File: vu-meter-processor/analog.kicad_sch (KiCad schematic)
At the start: 52 parts, among them U1 LM2904, U2 LM2904

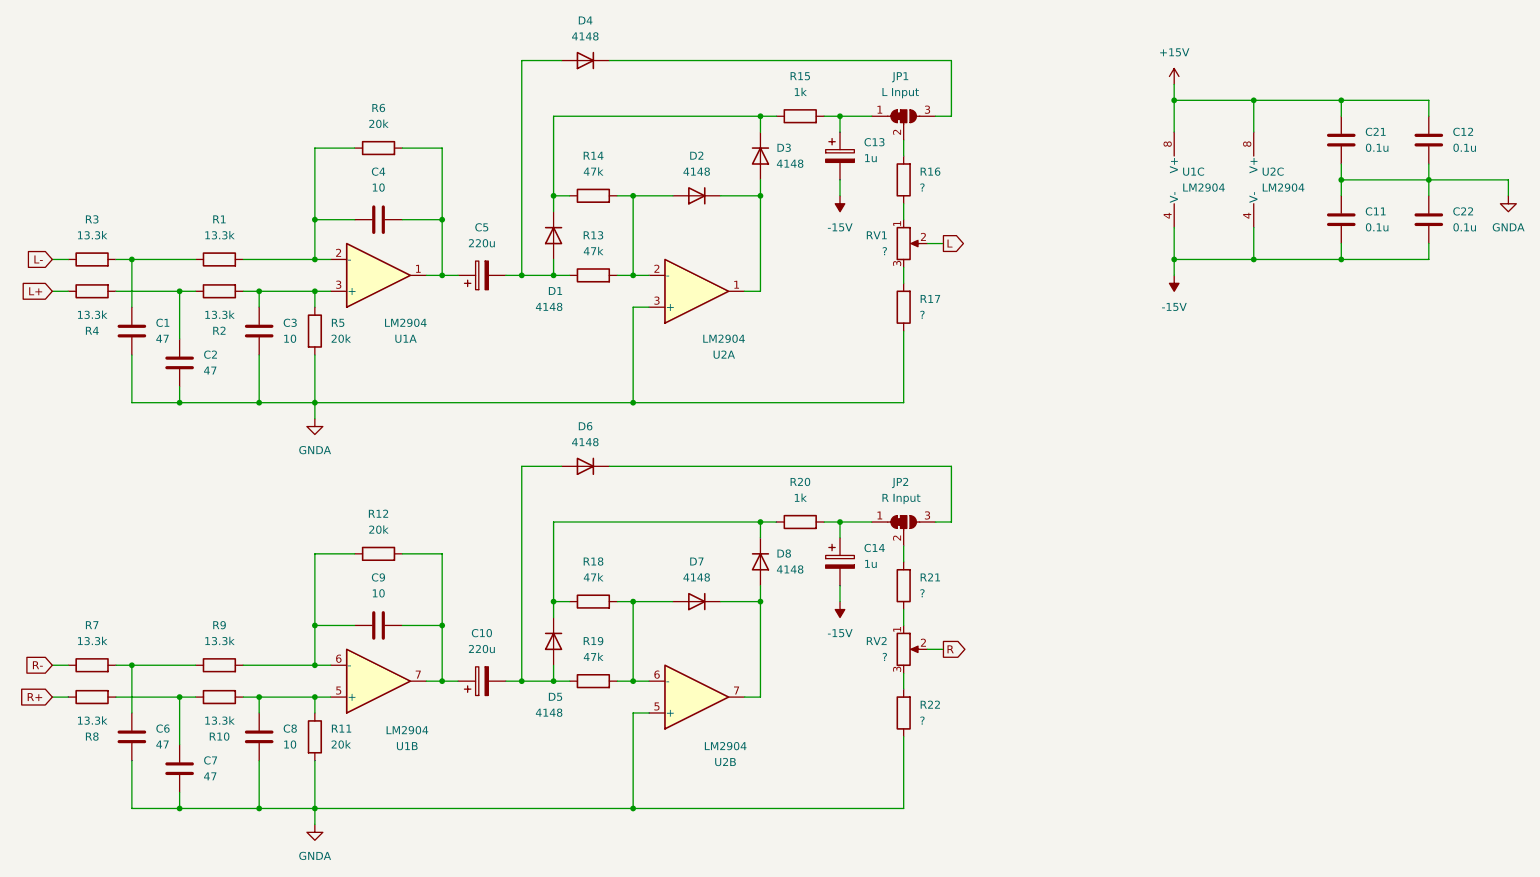
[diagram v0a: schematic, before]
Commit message: fix: change overall power supply to only 5V, make peak detector DNP for now
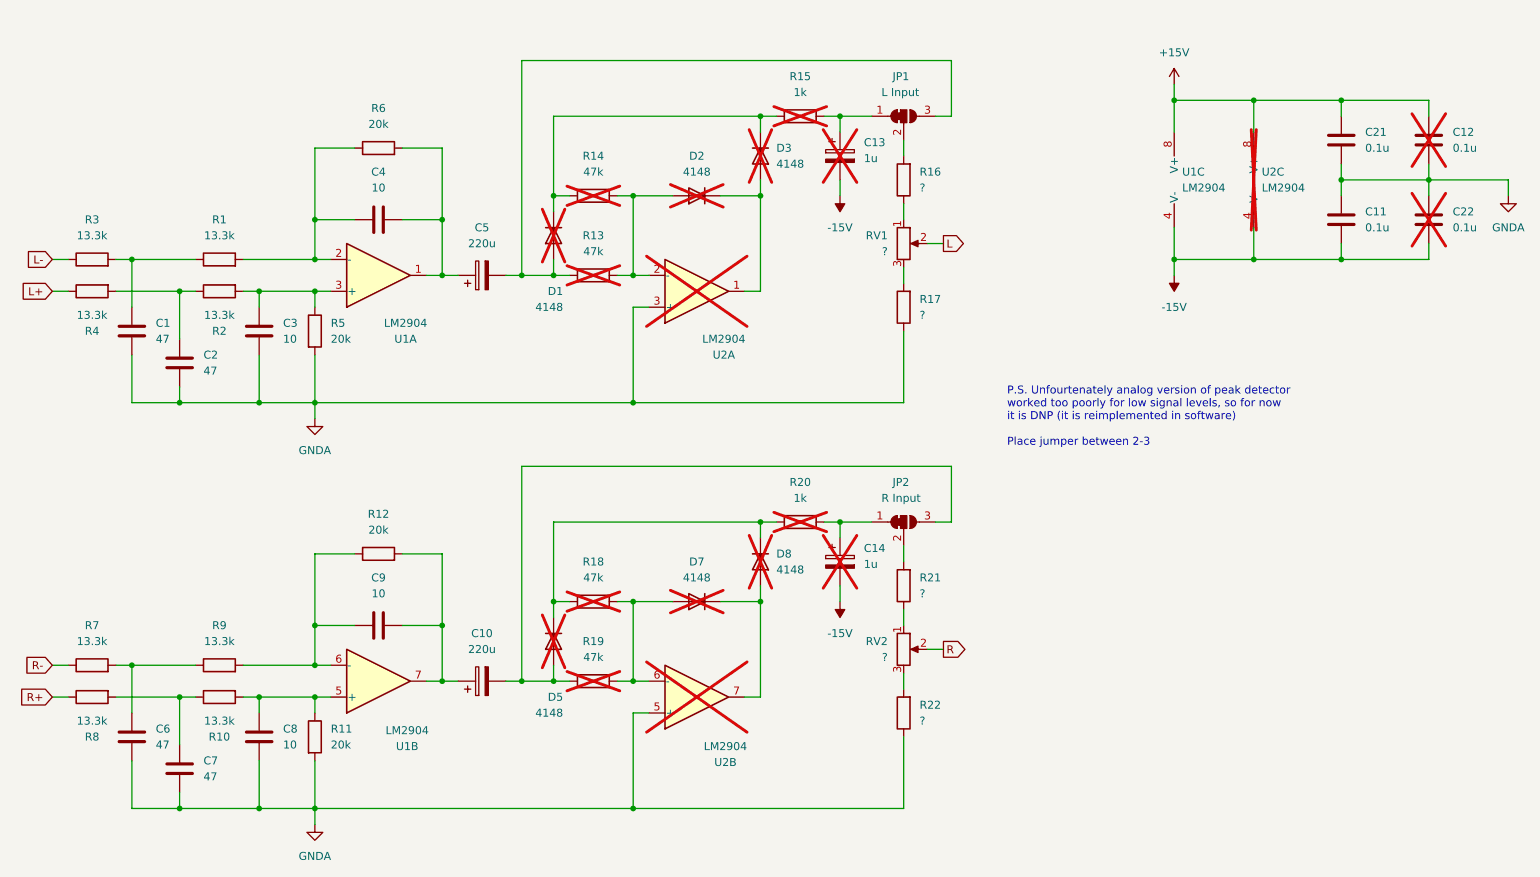
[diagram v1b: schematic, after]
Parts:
- removed D4, D6: 4148, Diode_SMD:D_MiniMELF, symbol Device:D
- C12, C13, C14, C22, D1, D2, D3, D5, D7, D8, R13, R14, R15, R18, R19, R20, U2: now not fitted
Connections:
- net at C10.2, D5.2 (A), R19.1: now also JP2.3 (B)
- net at C5.2, D1.2 (A), R13.1: now also JP1.3 (B)
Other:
- note added: "P.S. Unfourtenately analog version of peak detector worked too poorly for low signal levels, so for now it is DNP (it is reimplemented in software) Place jumper between 2-3"
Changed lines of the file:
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@@
 	(generator_version "9.0")
 	(paper "A4")
+	(text "P.S. Unfourtenately analog version of peak detector \nworked too poorly for low signal levels, so for now \nit is DNP (it is reimplemented in software)\n\nPlace jumper between 2-3"
+		(exclude_from_sim no)
+		(at 189.23 87.376 0)
+		(effects
+			(font
+				(size 1.27 1.27)
+			)
+			(justify left)
+		)
+	)
 	(junction
 		(at 242.57 49.53)
@@
 	(wire
 		(pts
-			(xy 118.11 95.25) (xy 111.76 95.25)
+			(xy 111.76 95.25) (xy 180.34 95.25)
 		)
 		(stroke
@@
 	(wire
 		(pts
-			(xy 125.73 95.25) (xy 180.34 95.25)
-		)
-		(stroke
-			(width 0)
-			(type default)
-		)
-	)
-	(wire
-		(pts
 			(xy 57.15 67.31) (xy 57.15 74.93)
 		)
@@
 	(wire
 		(pts
-			(xy 125.73 30.48) (xy 180.34 30.48)
-		)
-		(stroke
-			(width 0)
-			(type default)
-		)
-	)
-	(wire
-		(pts
 			(xy 172.72 85.09) (xy 172.72 73.66)
 		)
@@
 	(wire
 		(pts
-			(xy 118.11 30.48) (xy 111.76 30.48)
+			(xy 111.76 30.48) (xy 180.34 30.48)
 		)
 		(stroke
@@
 		(in_bom yes)
 		(on_board yes)
-		(dnp no)
+		(dnp yes)
 		(property "Reference" "U2"
 			(at 144.018 77.47 0)
@@
 		(in_bom yes)
 		(on_board yes)
-		(dnp no)
+		(dnp yes)
 		(fields_autoplaced yes)
 		(property "Reference" "R19"
@@
 		(in_bom yes)
 		(on_board yes)
-		(dnp no)
+		(dnp yes)
 		(fields_autoplaced yes)
 		(property "Reference" "D8"
@@
 		(in_bom yes)
 		(on_board yes)
-		(dnp no)
+		(dnp yes)
 		(fields_autoplaced yes)
 		(property "Reference" "R13"
@@
 		(in_bom yes)
 		(on_board yes)
-		(dnp no)
+		(dnp yes)
 		(fields_autoplaced yes)
 		(property "Reference" "C12"
@@
 		(in_bom yes)
 		(on_board yes)
-		(dnp no)
+		(dnp yes)
 		(fields_autoplaced yes)
 		(property "Reference" "R15"
@@
 		(in_bom yes)
 		(on_board yes)
-		(dnp no)
+		(dnp yes)
 		(fields_autoplaced yes)
 		(property "Reference" "D7"
@@
 		(in_bom yes)
 		(on_board yes)
-		(dnp no)
+		(dnp yes)
 		(fields_autoplaced yes)
 		(property "Reference" "C14"
@@
 		(in_bom yes)
 		(on_board yes)
-		(dnp no)
+		(dnp yes)
 		(fields_autoplaced yes)
 		(property "Reference" "R20"
@@
 	)
 	(symbol
-		(lib_id "Device:D")
-		(at 121.92 30.48 180)
-		(unit 1)
-		(exclude_from_sim no)
-		(in_bom yes)
-		(on_board yes)
-		(dnp no)
-		(fields_autoplaced yes)
-		(property "Reference" "D4"
-			(at 121.92 24.13 0)
-			(effects
-				(font
-					(size 1.27 1.27)
-				)
-			)
-		)
-		(property "Value" "4148"
-			(at 121.92 26.67 0)
-			(effects
-				(font
-					(size 1.27 1.27)
-				)
-			)
-		)
-		(property "Footprint" "Diode_SMD:D_MiniMELF"
-			(at 121.92 30.48 0)
-			(effects
-				(font
-					(size 1.27 1.27)
-				)
-				(hide yes)
-			)
-		)
-		(property "Datasheet" "~"
-			(at 121.92 30.48 0)
-			(effects
-				(font
-					(size 1.27 1.27)
-				)
-				(hide yes)
-			)
-		)
-		(property "Description" "Diode"
-			(at 121.92 30.48 0)
-			(effects
-				(font
-					(size 1.27 1.27)
-				)
-				(hide yes)
-			)
-		)
-		(property "Sim.Device" "D"
-			(at 121.92 30.48 0)
-			(effects
-				(font
-					(size 1.27 1.27)
-				)
-				(hide yes)
-			)
-		)
-		(property "Sim.Pins" "1=K 2=A"
-			(at 121.92 30.48 0)
-			(effects
-				(font
-					(size 1.27 1.27)
-				)
-				(hide yes)
-			)
-		)
-		(pin "1"
-		)
-		(pin "2"
-		)
-		(instances
-			(project "vu-meter-processor"
-				(path "/50201dbb-ce2c-4681-8d0b-b3063868b684/b5a15edd-f079-4332-a725-9b2801ef9020"
-					(reference "D4")
-					(unit 1)
-				)
-			)
-		)
-	)
-	(symbol
 		(lib_id "Device:R")
 		(at 123.19 52.07 90)
@@
 		(in_bom yes)
 		(on_board yes)
-		(dnp no)
+		(dnp yes)
 		(fields_autoplaced yes)
 		(property "Reference" "R14"
@@
 	)
 	(symbol
-		(lib_id "Device:D")
-		(at 121.92 95.25 180)
-		(unit 1)
-		(exclude_from_sim no)
-		(in_bom yes)
-		(on_board yes)
-		(dnp no)
-		(fields_autoplaced yes)
-		(property "Reference" "D6"
-			(at 121.92 88.9 0)
-			(effects
-				(font
-					(size 1.27 1.27)
-				)
-			)
-		)
-		(property "Value" "4148"
-			(at 121.92 91.44 0)
-			(effects
-				(font
-					(size 1.27 1.27)
-				)
-			)
-		)
-		(property "Footprint" "Diode_SMD:D_MiniMELF"
-			(at 121.92 95.25 0)
-			(effects
-				(font
-					(size 1.27 1.27)
-				)
-				(hide yes)
-			)
-		)
-		(property "Datasheet" "~"
-			(at 121.92 95.25 0)
-			(effects
-				(font
-					(size 1.27 1.27)
-				)
-				(hide yes)
-			)
-		)
-		(property "Description" "Diode"
-			(at 121.92 95.25 0)
-			(effects
-				(font
-					(size 1.27 1.27)
-				)
-				(hide yes)
-			)
-		)
-		(property "Sim.Device" "D"
-			(at 121.92 95.25 0)
-			(effects
-				(font
-					(size 1.27 1.27)
-				)
-				(hide yes)
-			)
-		)
-		(property "Sim.Pins" "1=K 2=A"
-			(at 121.92 95.25 0)
-			(effects
-				(font
-					(size 1.27 1.27)
-				)
-				(hide yes)
-			)
-		)
-		(pin "1"
-		)
-		(pin "2"
-		)
-		(instances
-			(project "vu-meter-processor"
-				(path "/50201dbb-ce2c-4681-8d0b-b3063868b684/b5a15edd-f079-4332-a725-9b2801ef9020"
-					(reference "D6")
-					(unit 1)
-				)
-			)
-		)
-	)
-	(symbol
 		(lib_id "Device:C_Polarized")
 		(at 105.41 64.77 90)
@@
 		(in_bom yes)
 		(on_board yes)
-		(dnp no)
+		(dnp yes)
 		(property "Reference" "D5"
 			(at 118.364 132.08 90)
@@
 		(in_bom yes)
 		(on_board yes)
-		(dnp no)
+		(dnp yes)
 		(fields_autoplaced yes)
 		(property "Reference" "C13"
@@
 		(in_bom yes)
 		(on_board yes)
-		(dnp no)
+		(dnp yes)
 		(fields_autoplaced yes)
 		(property "Reference" "U2"
@@
 		(in_bom yes)
 		(on_board yes)
-		(dnp no)
+		(dnp yes)
 		(fields_autoplaced yes)
 		(property "Reference" "R18"
@@
 		(in_bom yes)
 		(on_board yes)
-		(dnp no)
+		(dnp yes)
 		(fields_autoplaced yes)
 		(property "Reference" "D3"
@@
 		(in_bom yes)
 		(on_board yes)
-		(dnp no)
+		(dnp yes)
 		(property "Reference" "D1"
 			(at 118.364 67.31 90)
@@
 		(in_bom yes)
 		(on_board yes)
-		(dnp no)
+		(dnp yes)
 		(property "Reference" "U2"
 			(at 144.272 142.494 0)
@@
 		(in_bom yes)
 		(on_board yes)
-		(dnp no)
+		(dnp yes)
 		(fields_autoplaced yes)
 		(property "Reference" "C22"
@@
 		(in_bom yes)
 		(on_board yes)
-		(dnp no)
+		(dnp yes)
 		(fields_autoplaced yes)
 		(property "Reference" "D2"

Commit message: remove analog peak detector fully and split one chip into two for better inter-channel performance
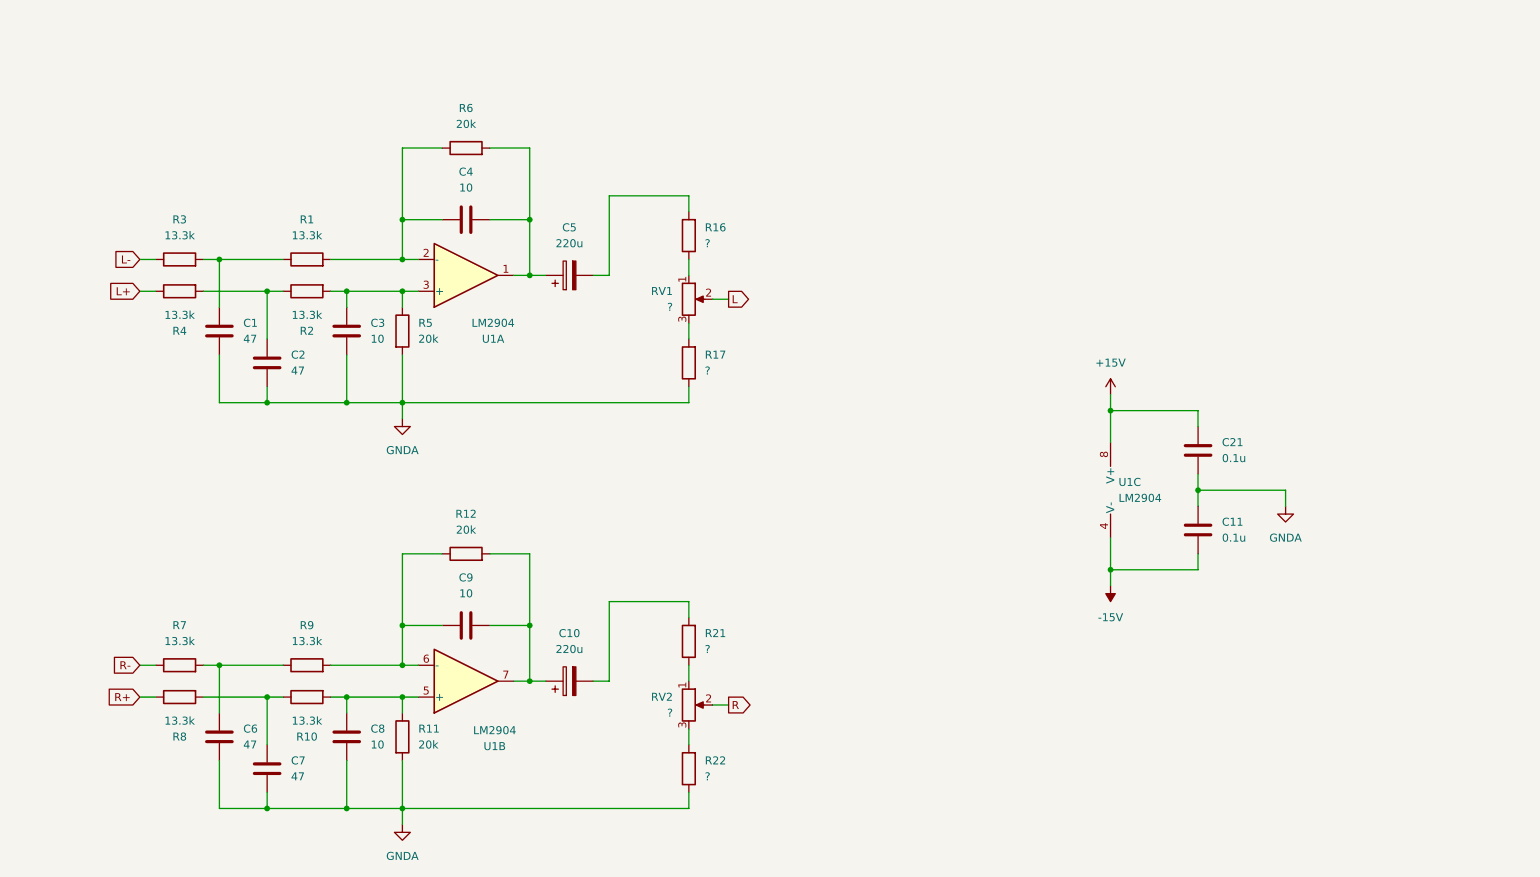
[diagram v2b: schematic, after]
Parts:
- removed C12, C22: 0.1u, Capacitor_SMD:C_0805_2012Metric, symbol Device:C
- removed C13, C14: 1u, Capacitor_THT:CP_Radial_D4.0mm_P1.50mm, symbol Device:C_Polarized
- removed D1, D2, D3, D5, D7, D8: 4148, Diode_SMD:D_MiniMELF, symbol Device:D
- removed JP1: L Input, Jumper:SolderJumper-3_P1.3mm_Open_Pad1.0x1.5mm, symbol Jumper:SolderJumper_3_Bridged12
- removed JP2: R Input, Jumper:SolderJumper-3_P1.3mm_Open_Pad1.0x1.5mm, symbol Jumper:SolderJumper_3_Bridged12
- removed R13, R14, R18, R19: 47k, Resistor_SMD:R_0805_2012Metric, symbol Device:R
- removed R15, R20: 1k, Resistor_SMD:R_0805_2012Metric, symbol Device:R
- removed U2: LM2904, Package_SO:SOP-8_3.9x4.9mm_P1.27mm, symbol Amplifier_Operational:LM2904
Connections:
- net at C10.2: now also R21.2
- net at C5.2: now also R16.2
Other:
- note removed: "P.S. Unfourtenately analog version of peak detector worked too poorly for low signal levels, so for now it is DNP (it is reimplemented in software) Place jumper between 2-3"
- moved on the sheet: C1, C10, C11, C2, C21, C3, C4, C5, C6, C7, C8, C9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
